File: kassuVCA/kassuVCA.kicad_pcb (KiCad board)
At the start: 2 copper layers, 140 parts, among them J201 Conn_02x05_Odd_Even, Q401 MMBT3904, Q402 MBT3904DW1, Q403 MBT3904DW1, Q404 MMBT3904, Q501 MMBT3904, Q502 MMBT3904, Q503 MBT3904DW1, Q504 MBT3904DW1, SW401 SW_DPDT_x2, SW402 SW_DPDT_x2, SW501 SW_DPDT_x2, SW502 SW_DPDT_x2, U301 TL074, U401 TL072, U402 TL072, U501 TL072, U502 TL072

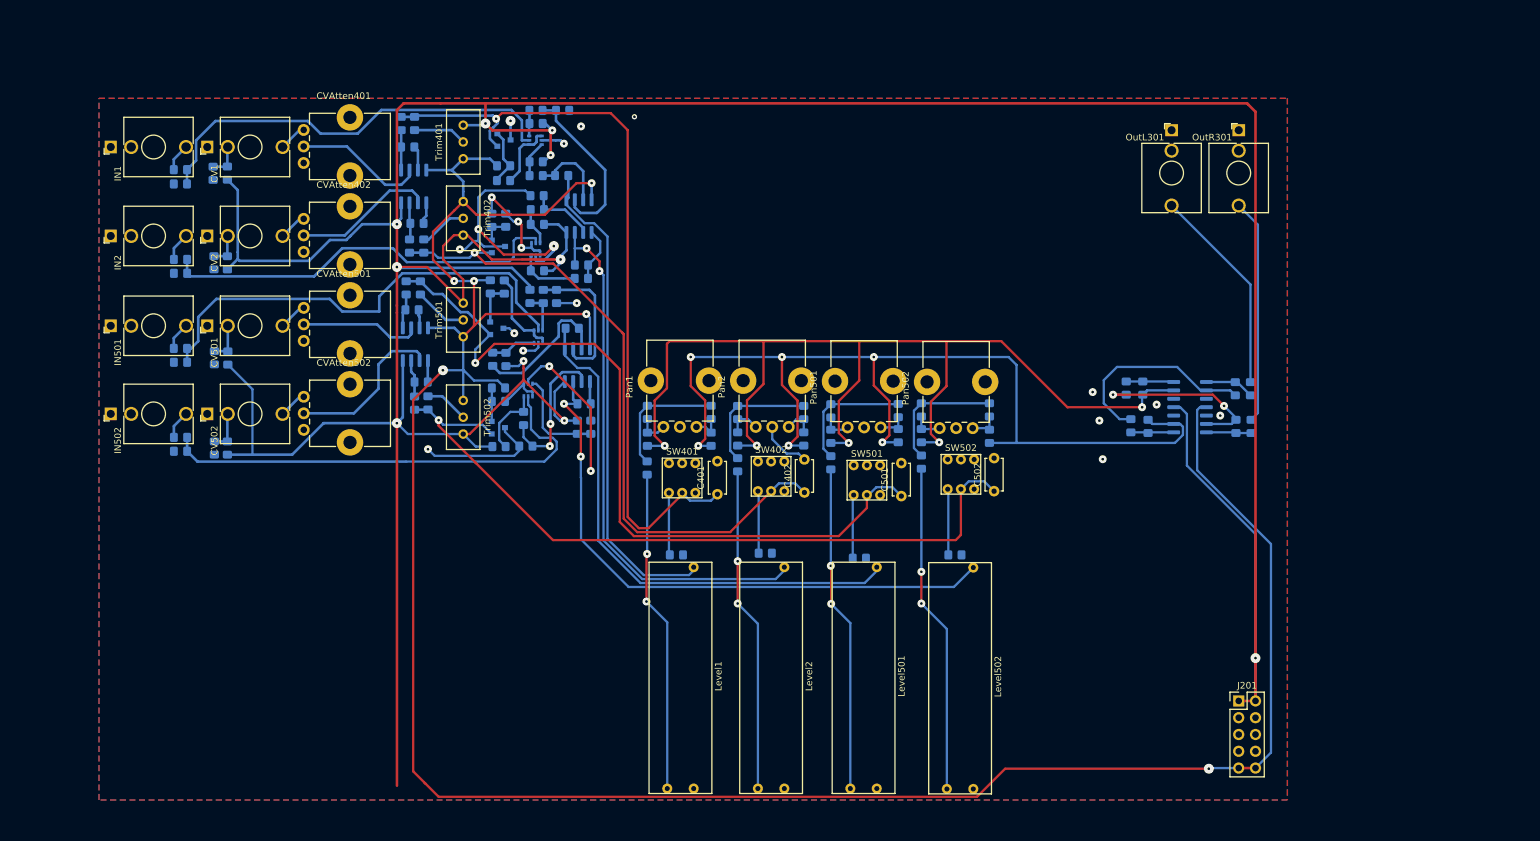
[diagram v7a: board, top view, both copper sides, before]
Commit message: mixer WIP, 8 channels, more or less
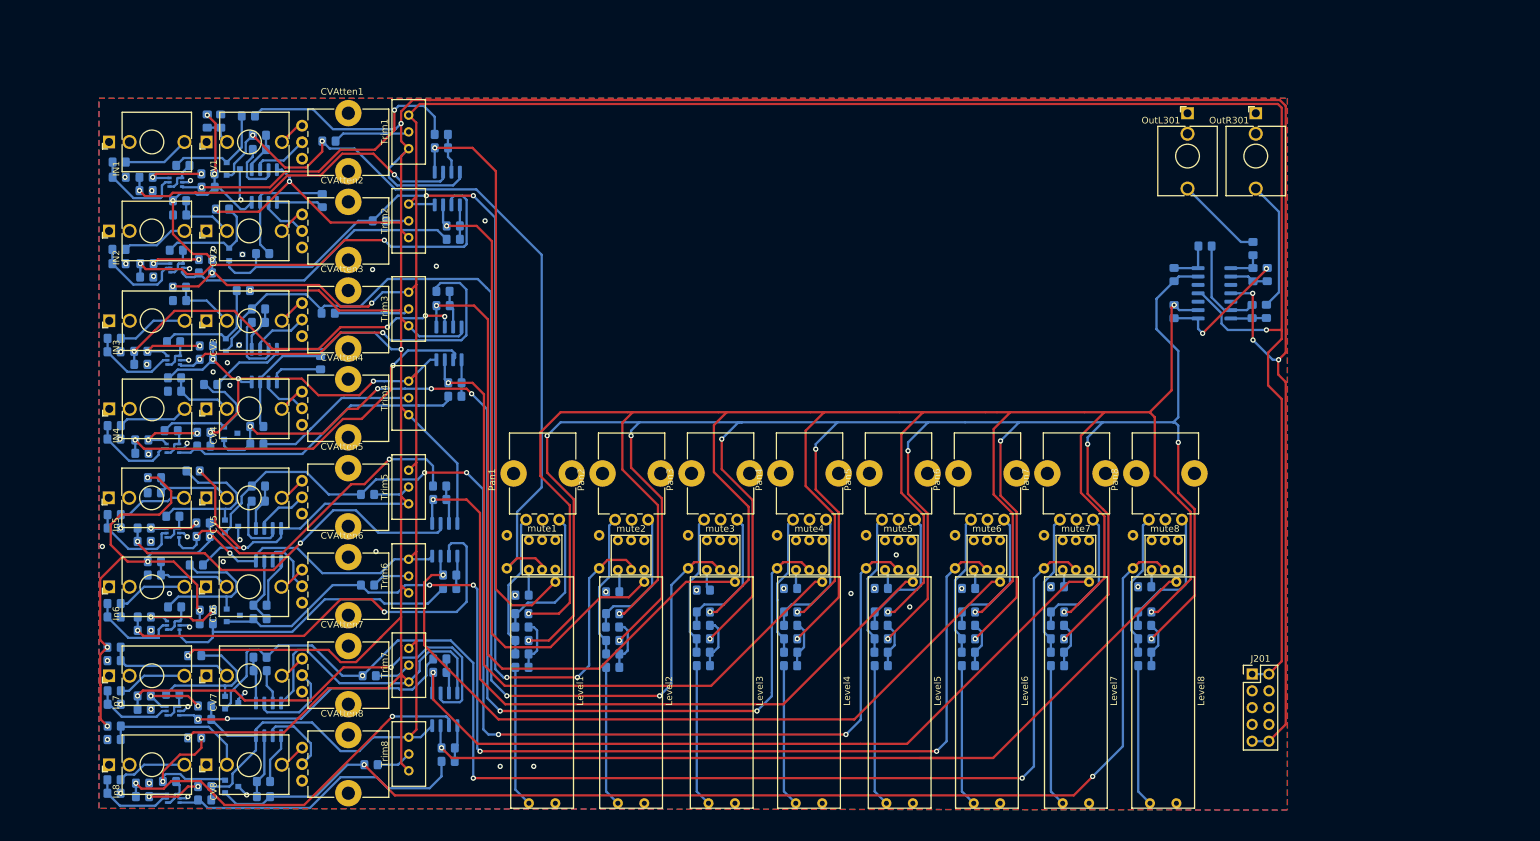
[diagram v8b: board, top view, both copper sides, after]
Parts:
- removed CV501, CV502, IN501, IN502: AudioJack2_SwitchT, Connector_Audio:Jack_3.5mm_QingPu_WQP-PJ398SM_Vertical_CircularHoles
- removed CVAtten401, CVAtten402, CVAtten501, CVAtten502, Pan501, Pan502: 100K, Potentiometer_THT:Potentiometer_Alps_RK09K_Single_Vertical
- removed Level501, Level502: 100K, MixerFootprints:A-1623_SlidePot
- removed SW401, SW402, SW501, SW502: SW_DPDT_x2, MixerFootprints:A-330-6mm-dpdt
- removed Trim401, Trim402, Trim501, Trim502: 100K, Potentiometer_THT:Potentiometer_Bourns_3296W_Vertical
- added C1: C, Capacitor_THT:C_Disc_D4.7mm_W2.5mm_P5.00mm, B.Cu at (141.7, 96.8)
- added C2: C, Capacitor_THT:C_Disc_D4.7mm_W2.5mm_P5.00mm, B.Cu at (155.2, 96.8)
- added C3: C, Capacitor_THT:C_Disc_D4.7mm_W2.5mm_P5.00mm, B.Cu at (168.7, 96.8)
- added C4: C, Capacitor_THT:C_Disc_D4.7mm_W2.5mm_P5.00mm, B.Cu at (182.1, 96.8)
- added CV3: AudioJack2_SwitchT, Connector_Audio:Jack_3.5mm_QingPu_WQP-PJ398SM_Vertical_CircularHoles, F.Cu at (41.9, 59.3)
- added CV4: AudioJack2_Switch, Connector_Audio:Jack_3.5mm_QingPu_WQP-PJ398SM_Vertical_CircularHoles, F.Cu at (41.9, 72.6)
- added CV5: AudioJack2_SwitchT, Connector_Audio:Jack_3.5mm_QingPu_WQP-PJ398SM_Vertical_CircularHoles, F.Cu at (41.9, 86.1)
- added CV6: AudioJack2_SwitchT, Connector_Audio:Jack_3.5mm_QingPu_WQP-PJ398SM_Vertical_CircularHoles, F.Cu at (41.9, 99.6)
- added CV7: AudioJack2_SwitchT, Connector_Audio:Jack_3.5mm_QingPu_WQP-PJ398SM_Vertical_CircularHoles, F.Cu at (41.9, 113.0)
- added CV8: AudioJack2_SwitchT, Connector_Audio:Jack_3.5mm_QingPu_WQP-PJ398SM_Vertical_CircularHoles, F.Cu at (41.9, 126.5)
- added CVAtten1: 100K, Potentiometer_THT:Potentiometer_Alps_RK09K_Single_Vertical, F.Cu at (56.4, 34.8)
- added CVAtten2: 100K, Potentiometer_THT:Potentiometer_Alps_RK09K_Single_Vertical, F.Cu at (56.4, 48.2)
- added CVAtten3: 100K, Potentiometer_THT:Potentiometer_Alps_RK09K_Single_Vertical, F.Cu at (56.4, 61.6)
- added CVAtten4: 100K, Potentiometer_THT:Potentiometer_Alps_RK09K_Single_Vertical, F.Cu at (56.4, 75.1)
- added CVAtten5: 100K, Potentiometer_THT:Potentiometer_Alps_RK09K_Single_Vertical, F.Cu at (56.4, 88.5)
- added CVAtten6: 100K, Potentiometer_THT:Potentiometer_Alps_RK09K_Single_Vertical, F.Cu at (56.4, 102.0)
- added CVAtten7: 100K, Potentiometer_THT:Potentiometer_Alps_RK09K_Single_Vertical, F.Cu at (56.4, 115.4)
- added CVAtten8: 100K, Potentiometer_THT:Potentiometer_Alps_RK09K_Single_Vertical, F.Cu at (56.4, 128.9)
- added IN3: AudioJack2_SwitchT, Connector_Audio:Jack_3.5mm_QingPu_WQP-PJ398SM_Vertical_CircularHoles, F.Cu at (27.2, 59.3)
- added IN4: AudioJack2_SwitchT, Connector_Audio:Jack_3.5mm_QingPu_WQP-PJ398SM_Vertical_CircularHoles, F.Cu at (27.2, 72.6)
- added In5: AudioJack2_SwitchT, Connector_Audio:Jack_3.5mm_QingPu_WQP-PJ398SM_Vertical_CircularHoles, F.Cu at (27.1, 86.1)
- added In6: AudioJack2_SwitchT, Connector_Audio:Jack_3.5mm_QingPu_WQP-PJ398SM_Vertical_CircularHoles, F.Cu at (27.2, 99.6)
- added In7: AudioJack2_SwitchT, Connector_Audio:Jack_3.5mm_QingPu_WQP-PJ398SM_Vertical_CircularHoles, F.Cu at (27.2, 113.0)
- added In8: AudioJack2_SwitchT, Connector_Audio:Jack_3.5mm_QingPu_WQP-PJ398SM_Vertical_CircularHoles, F.Cu at (27.2, 126.5)
- added Level3: 100K, MixerFootprints:A-1623_SlidePot, F.Cu at (119.9, 115.6)
- added Level4: 100K, MixerFootprints:A-1623_SlidePot, F.Cu at (133.1, 115.6)
- added Level5: 100K, MixerFootprints:A-1623_SlidePot, F.Cu at (146.8, 115.6)
- added Level6: 100K, MixerFootprints:A-1623_SlidePot, F.Cu at (160.0, 115.6)
- added Level7: 100K, MixerFootprints:A-1623_SlidePot, F.Cu at (173.5, 115.6)
- added Level8: 100K, MixerFootprints:A-1623_SlidePot, F.Cu at (186.7, 115.6)
- added Pan3: 100K, Potentiometer_THT:Potentiometer_Alps_RK09K_Single_Vertical, F.Cu at (122.2, 89.4)
- added Pan4: 100K, Potentiometer_THT:Potentiometer_Alps_RK09K_Single_Vertical, F.Cu at (135.7, 89.4)
- added Pan5: 100K, Potentiometer_THT:Potentiometer_Alps_RK09K_Single_Vertical, F.Cu at (149.1, 89.4)
- added Pan6: 100K, Potentiometer_THT:Potentiometer_Alps_RK09K_Single_Vertical, F.Cu at (162.6, 89.4)
- added Pan7: 100K, Potentiometer_THT:Potentiometer_Alps_RK09K_Single_Vertical, F.Cu at (176.1, 89.4)
- added Pan8: 100K, Potentiometer_THT:Potentiometer_Alps_RK09K_Single_Vertical, F.Cu at (189.5, 89.4)
- added Q1: MMBT3904, Package_TO_SOT_SMD:SOT-23, B.Cu at (45.7, 90.4)
- added Q2: MMBT3904, Package_TO_SOT_SMD:SOT-23, B.Cu at (46.0, 103.9)
- added Q3: MBT3904DW1, Package_TO_SOT_SMD:SOT-363_SC-70-6, B.Cu at (36.8, 91.4)
- added Q4: MBT3904DW1, Package_TO_SOT_SMD:SOT-363_SC-70-6, B.Cu at (36.9, 105.4)
- added Q5: MMBT3904, Package_TO_SOT_SMD:SOT-23, B.Cu at (45.7, 117.1)
- added Q6: MMBT3904, Package_TO_SOT_SMD:SOT-23, B.Cu at (45.7, 129.8)
- added Q7: MBT3904DW1, Package_TO_SOT_SMD:SOT-363_SC-70-6, B.Cu at (36.8, 118.4)
- added Q8: MBT3904DW1, Package_TO_SOT_SMD:SOT-363_SC-70-6, B.Cu at (36.9, 131.6)
- added R1: 220K, Resistor_SMD:R_0805_2012Metric_Pad1.20x1.40mm_HandSolder, B.Cu at (34.1, 83.1)
- added R10: 22K, Resistor_SMD:R_0805_2012Metric_Pad1.20x1.40mm_HandSolder, B.Cu at (50.0, 104.4)
- added R11: 22K, Resistor_SMD:R_0805_2012Metric_Pad1.20x1.40mm_HandSolder, B.Cu at (66.3, 85.6)
- added R12: 22K, Resistor_SMD:R_0805_2012Metric_Pad1.20x1.40mm_HandSolder, B.Cu at (66.3, 99.3)
- added R13: 1K, Resistor_SMD:R_0805_2012Metric_Pad1.20x1.40mm_HandSolder, B.Cu at (28.0, 90.7)
- added R14: 1K, Resistor_SMD:R_0805_2012Metric_Pad1.20x1.40mm_HandSolder, B.Cu at (144.0, 99.8)
- added R15: 1K, Resistor_SMD:R_0805_2012Metric_Pad1.20x1.40mm_HandSolder, B.Cu at (27.9, 104.1)
- added R16: 1K, Resistor_SMD:R_0805_2012Metric_Pad1.20x1.40mm_HandSolder, B.Cu at (157.2, 99.8)
- added R17: 10K, Resistor_SMD:R_0805_2012Metric_Pad1.20x1.40mm_HandSolder, B.Cu at (41.4, 91.9)
- added R18: 10K, Resistor_SMD:R_0805_2012Metric_Pad1.20x1.40mm_HandSolder, B.Cu at (41.9, 105.2)
- added R19: 22K, Resistor_SMD:R_0805_2012Metric_Pad1.20x1.40mm_HandSolder, B.Cu at (36.8, 88.9)
- added R2: 220K, Resistor_SMD:R_0805_2012Metric_Pad1.20x1.40mm_HandSolder, B.Cu at (34.0, 95.8)
- added R20: 10K, Resistor_SMD:R_0805_2012Metric_Pad1.20x1.40mm_HandSolder, B.Cu at (39.9, 82.0)
- added R21: 22K, Resistor_SMD:R_0805_2012Metric_Pad1.20x1.40mm_HandSolder, B.Cu at (37.1, 102.6)
- added R22: 10K, Resistor_SMD:R_0805_2012Metric_Pad1.20x1.40mm_HandSolder, B.Cu at (40.4, 96.3)
- added R23: 10K, Resistor_SMD:R_0805_2012Metric_Pad1.20x1.40mm_HandSolder, B.Cu at (41.4, 89.9)
- added R24: 10K, Resistor_SMD:R_0805_2012Metric_Pad1.20x1.40mm_HandSolder, B.Cu at (41.9, 103.1)
- added R25: 10K, Resistor_SMD:R_0805_2012Metric_Pad1.20x1.40mm_HandSolder, B.Cu at (77.2, 84.3)
- added R26: 10K, Resistor_SMD:R_0805_2012Metric_Pad1.20x1.40mm_HandSolder, B.Cu at (32.5, 90.7)
- added R27: 10K, Resistor_SMD:R_0805_2012Metric_Pad1.20x1.40mm_HandSolder, B.Cu at (78.7, 99.8)
- added R28: 10K, Resistor_SMD:R_0805_2012Metric_Pad1.20x1.40mm_HandSolder, B.Cu at (32.5, 104.1)
- added R29: 220K, Resistor_SMD:R_0805_2012Metric_Pad1.20x1.40mm_HandSolder, B.Cu at (32.5, 92.7)
- added R3: 100K, Resistor_SMD:R_0805_2012Metric_Pad1.20x1.40mm_HandSolder, B.Cu at (34.0, 85.3)
- added R30: 220K, Resistor_SMD:R_0805_2012Metric_Pad1.20x1.40mm_HandSolder, B.Cu at (32.5, 106.2)
- added R31: 220K, Resistor_SMD:R_0805_2012Metric_Pad1.20x1.40mm_HandSolder, B.Cu at (77.2, 86.4)
- added R32: 220K, Resistor_SMD:R_0805_2012Metric_Pad1.20x1.40mm_HandSolder, B.Cu at (78.7, 97.8)
- added R33: 220K, Resistor_SMD:R_0805_2012Metric_Pad1.20x1.40mm_HandSolder, B.Cu at (144.0, 111.5)
- added R34: 220K, Resistor_SMD:R_0805_2012Metric_Pad1.20x1.40mm_HandSolder, B.Cu at (157.2, 111.5)
- added R35: 22K, Resistor_SMD:R_0805_2012Metric_Pad1.20x1.40mm_HandSolder, B.Cu at (144.0, 109.5)
- added R36: 22K, Resistor_SMD:R_0805_2012Metric_Pad1.20x1.40mm_HandSolder, B.Cu at (144.0, 105.4)
- added R37: 22K, Resistor_SMD:R_0805_2012Metric_Pad1.20x1.40mm_HandSolder, B.Cu at (157.2, 109.5)
- added R38: 22K, Resistor_SMD:R_0805_2012Metric_Pad1.20x1.40mm_HandSolder, B.Cu at (157.2, 105.4)
- added R39: 22K, Resistor_SMD:R_0805_2012Metric_Pad1.20x1.40mm_HandSolder, B.Cu at (144.0, 107.4)
- added R4: 100K, Resistor_SMD:R_0805_2012Metric_Pad1.20x1.40mm_HandSolder, B.Cu at (34.0, 97.8)
- added R40: 22K, Resistor_SMD:R_0805_2012Metric_Pad1.20x1.40mm_HandSolder, B.Cu at (144.0, 103.4)
- added R41: 22K, Resistor_SMD:R_0805_2012Metric_Pad1.20x1.40mm_HandSolder, B.Cu at (157.2, 107.4)
- added R42: 22K, Resistor_SMD:R_0805_2012Metric_Pad1.20x1.40mm_HandSolder, B.Cu at (157.2, 103.4)
- added R43: 220K, Resistor_SMD:R_0805_2012Metric_Pad1.20x1.40mm_HandSolder, B.Cu at (27.9, 108.7)
- added R44: 220K, Resistor_SMD:R_0805_2012Metric_Pad1.20x1.40mm_HandSolder, B.Cu at (28.0, 120.7)
- added R45: 100K, Resistor_SMD:R_0805_2012Metric_Pad1.20x1.40mm_HandSolder, B.Cu at (27.9, 110.7)
- added R46: 100K, Resistor_SMD:R_0805_2012Metric_Pad1.20x1.40mm_HandSolder, B.Cu at (27.9, 122.7)
- added R47: 220K, Resistor_SMD:R_0805_2012Metric_Pad1.20x1.40mm_HandSolder, B.Cu at (28.0, 115.3)
- added R48: 220K, Resistor_SMD:R_0805_2012Metric_Pad1.20x1.40mm_HandSolder, B.Cu at (27.9, 128.8)
- added R49: 47K, Resistor_SMD:R_0805_2012Metric_Pad1.20x1.40mm_HandSolder, B.Cu at (50.0, 112.3)
- added R5: 220K, Resistor_SMD:R_0805_2012Metric_Pad1.20x1.40mm_HandSolder, B.Cu at (28.0, 88.6)
- added R50: 47K, Resistor_SMD:R_0805_2012Metric_Pad1.20x1.40mm_HandSolder, B.Cu at (50.5, 129.0)
- added R51: 22K, Resistor_SMD:R_0805_2012Metric_Pad1.20x1.40mm_HandSolder, B.Cu at (50.0, 110.2)
- added R52: 22K, Resistor_SMD:R_0805_2012Metric_Pad1.20x1.40mm_HandSolder, B.Cu at (50.5, 131.3)
- added R53: 22K, Resistor_SMD:R_0805_2012Metric_Pad1.20x1.40mm_HandSolder, B.Cu at (66.5, 113.0)
- added R54: 22K, Resistor_SMD:R_0805_2012Metric_Pad1.20x1.40mm_HandSolder, B.Cu at (66.8, 126.5)
- added R55: 1K, Resistor_SMD:R_0805_2012Metric_Pad1.20x1.40mm_HandSolder, B.Cu at (28.0, 117.3)
- added R56: 1K, Resistor_SMD:R_0805_2012Metric_Pad1.20x1.40mm_HandSolder, B.Cu at (170.7, 99.6)
- added R57: 1K, Resistor_SMD:R_0805_2012Metric_Pad1.20x1.40mm_HandSolder, B.Cu at (27.9, 130.8)
- added R58: 1K, Resistor_SMD:R_0805_2012Metric_Pad1.20x1.40mm_HandSolder, B.Cu at (183.9, 99.6)
- added R59: 10K, Resistor_SMD:R_0805_2012Metric_Pad1.20x1.40mm_HandSolder, B.Cu at (41.6, 119.6)
- added R6: 220K, Resistor_SMD:R_0805_2012Metric_Pad1.20x1.40mm_HandSolder, B.Cu at (27.9, 102.1)
- added R60: 10K, Resistor_SMD:R_0805_2012Metric_Pad1.20x1.40mm_HandSolder, B.Cu at (41.6, 131.8)
- added R61: 22K, Resistor_SMD:R_0805_2012Metric_Pad1.20x1.40mm_HandSolder, B.Cu at (36.8, 115.8)
- added R62: 10K, Resistor_SMD:R_0805_2012Metric_Pad1.20x1.40mm_HandSolder, B.Cu at (40.1, 110.0)
- added R63: 22K, Resistor_SMD:R_0805_2012Metric_Pad1.20x1.40mm_HandSolder, B.Cu at (36.3, 129.0)
- added R64: 10K, Resistor_SMD:R_0805_2012Metric_Pad1.20x1.40mm_HandSolder, B.Cu at (40.1, 122.4)
- added R65: 10K, Resistor_SMD:R_0805_2012Metric_Pad1.20x1.40mm_HandSolder, B.Cu at (41.6, 117.6)
- added R66: 10K, Resistor_SMD:R_0805_2012Metric_Pad1.20x1.40mm_HandSolder, B.Cu at (41.6, 129.8)
- added R67: 10K, Resistor_SMD:R_0805_2012Metric_Pad1.20x1.40mm_HandSolder, B.Cu at (77.2, 110.5)
- added R68: 10K, Resistor_SMD:R_0805_2012Metric_Pad1.20x1.40mm_HandSolder, B.Cu at (32.5, 116.1)
- added R69: 10K, Resistor_SMD:R_0805_2012Metric_Pad1.20x1.40mm_HandSolder, B.Cu at (78.5, 126.0)
- added R7: 47K, Resistor_SMD:R_0805_2012Metric_Pad1.20x1.40mm_HandSolder, B.Cu at (49.8, 86.6)
- added R70: 10K, Resistor_SMD:R_0805_2012Metric_Pad1.20x1.40mm_HandSolder, B.Cu at (32.2, 131.3)
- added R71: 220K, Resistor_SMD:R_0805_2012Metric_Pad1.20x1.40mm_HandSolder, B.Cu at (32.5, 118.1)
- added R72: 220K, Resistor_SMD:R_0805_2012Metric_Pad1.20x1.40mm_HandSolder, B.Cu at (32.2, 129.3)
- added R73: 220K, Resistor_SMD:R_0805_2012Metric_Pad1.20x1.40mm_HandSolder, B.Cu at (77.2, 112.5)
- added R74: 220K, Resistor_SMD:R_0805_2012Metric_Pad1.20x1.40mm_HandSolder, B.Cu at (78.5, 124.0)
- added R75: 220K, Resistor_SMD:R_0805_2012Metric_Pad1.20x1.40mm_HandSolder, B.Cu at (170.7, 111.5)
- added R76: 220K, Resistor_SMD:R_0805_2012Metric_Pad1.20x1.40mm_HandSolder, B.Cu at (183.9, 111.5)
- added R77: 22K, Resistor_SMD:R_0805_2012Metric_Pad1.20x1.40mm_HandSolder, B.Cu at (170.7, 109.5)
- added R78: 22K, Resistor_SMD:R_0805_2012Metric_Pad1.20x1.40mm_HandSolder, B.Cu at (170.7, 105.4)
- added R79: 22K, Resistor_SMD:R_0805_2012Metric_Pad1.20x1.40mm_HandSolder, B.Cu at (183.9, 109.5)
- added R8: 47K, Resistor_SMD:R_0805_2012Metric_Pad1.20x1.40mm_HandSolder, B.Cu at (50.0, 102.4)
- added R80: 22K, Resistor_SMD:R_0805_2012Metric_Pad1.20x1.40mm_HandSolder, B.Cu at (183.9, 105.4)
- added R81: 22K, Resistor_SMD:R_0805_2012Metric_Pad1.20x1.40mm_HandSolder, B.Cu at (170.7, 107.4)
- added R82: 22K, Resistor_SMD:R_0805_2012Metric_Pad1.20x1.40mm_HandSolder, B.Cu at (170.7, 103.4)
- added R83: 22K, Resistor_SMD:R_0805_2012Metric_Pad1.20x1.40mm_HandSolder, B.Cu at (183.9, 107.4)
- added R84: 22K, Resistor_SMD:R_0805_2012Metric_Pad1.20x1.40mm_HandSolder, B.Cu at (183.9, 103.4)
- added R9: 22K, Resistor_SMD:R_0805_2012Metric_Pad1.20x1.40mm_HandSolder, B.Cu at (49.8, 84.3)
- added Trim1: 100K, Potentiometer_THT:Potentiometer_Bourns_3296W_Vertical, F.Cu at (72.5, 28.2)
- added Trim2: 100K, Potentiometer_THT:Potentiometer_Bourns_3296W_Vertical, F.Cu at (72.5, 41.7)
- added Trim3: 100K, Potentiometer_THT:Potentiometer_Bourns_3296W_Vertical, F.Cu at (72.5, 55.0)
- added Trim4: 100K, Potentiometer_THT:Potentiometer_Bourns_3296W_Vertical, F.Cu at (72.5, 68.5)
- added Trim5: 100K, Potentiometer_THT:Potentiometer_Bourns_3296W_Vertical, F.Cu at (72.5, 81.9)
- added Trim6: 100K, Potentiometer_THT:Potentiometer_Bourns_3296W_Vertical, F.Cu at (72.5, 95.4)
- added Trim7: 100K, Potentiometer_THT:Potentiometer_Bourns_3296W_Vertical, F.Cu at (72.5, 108.9)
- added Trim8: 100K, Potentiometer_THT:Potentiometer_Bourns_3296W_Vertical, F.Cu at (72.5, 122.3)
- added U1: TL072, Package_SO:SOIC-8_3.9x4.9mm_P1.27mm, B.Cu at (51.3, 93.2)
- added U2: TL072, Package_SO:SOIC-8_3.9x4.9mm_P1.27mm, B.Cu at (78.0, 92.5)
- added U3: TL072, Package_SO:SOIC-8_3.9x4.9mm_P1.27mm, B.Cu at (51.3, 119.6)
- added U4: TL072, Package_SO:SOIC-8_3.9x4.9mm_P1.27mm, B.Cu at (78.0, 118.1)
- added mute1: SW_DPDT_x2, MixerFootprints:A-330-6mm-dpdt, F.Cu at (92.7, 94.7)
- added mute2: SW_DPDT_x2, MixerFootprints:A-330-6mm-dpdt, F.Cu at (106.2, 94.8)
- added mute3: SW_DPDT_x2, MixerFootprints:A-330-6mm-dpdt, F.Cu at (119.6, 94.8)
- added mute4: SW_DPDT_x2, MixerFootprints:A-330-6mm-dpdt, F.Cu at (133.1, 94.8)
- added mute5: mute5, MixerFootprints:A-330-6mm-dpdt, F.Cu at (146.6, 94.8)
- added mute6: SW_DPDT_x2, MixerFootprints:A-330-6mm-dpdt, F.Cu at (160.0, 94.8)
- added mute7: mute7, MixerFootprints:A-330-6mm-dpdt, F.Cu at (173.5, 94.8)
- added mute8: SW_DPDT_x2, MixerFootprints:A-330-6mm-dpdt, F.Cu at (186.9, 94.8)
- C401, C402, C501, C502: moved to B.Cu
- CV2: value AudioJack2_SwitchT -> AudioJack2_Switch
- moved R429 64.2 mm to (32.8, 39.6)
- moved R529 63.7 mm to (32.0, 65.9), turned to 180 degrees
- moved R526 61.5 mm to (32.0, 63.9), turned to 0 degrees
- moved R430 60.3 mm to (32.9, 52.7), turned to 180 degrees
- moved R426 59.9 mm to (32.8, 37.6), turned to 0 degrees
- moved R428 59.6 mm to (32.9, 50.7), turned to 0 degrees
- moved R530 58.1 mm to (32.1, 79.4), turned to 180 degrees
- moved R528 57.9 mm to (32.1, 77.3), turned to 0 degrees
- moved R518 56.6 mm to (41.5, 78.3), turned to 180 degrees
- moved Q503 55.3 mm to (37.0, 65.3), turned to 0 degrees
- moved Q402 54.8 mm to (37.3, 38.4)
- moved Q504 54.5 mm to (36.8, 78.6), turned to 0 degrees
- moved Q403 54.4 mm to (37.4, 51.3), turned to 0 degrees
- moved R519 50.7 mm to (36.9, 62.5), turned to 180 degrees
- moved R424 50.5 mm to (41.8, 50.0)
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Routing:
- net -12V: track 382.8 -> 693.1 mm, vias 7 -> 12
- net Level1R: track 162.4 -> 426.2 mm, vias 5 -> 16
- net Level1L: track 149.0 -> 401.6 mm, vias 6 -> 9
- net Net-(C3-Pad1): track 0.00 -> 190.4 mm, vias 0 -> 3
- net Net-(C4-Pad1): track 0.00 -> 177.3 mm, vias 0 -> 2
- net Net-(C1-Pad1): track 0.00 -> 172.1 mm, vias 0 -> 4
- net Net-(C2-Pad1): track 0.00 -> 170.7 mm, vias 0 -> 4
- net Net-(Level8-Pad3): track 0.00 -> 131.9 mm, vias 0 -> 1
- net Net-(Level7-Pad3): track 0.00 -> 119.5 mm, vias 0 -> 1
- net Net-(Level6-Pad3): track 0.00 -> 116.2 mm, vias 0 -> 1
- net Net-(Level5-Pad3): track 0.00 -> 111.5 mm, vias 0 -> 1
- net GND: track 106.1 -> 22.2 mm, vias 18 -> 55
- net Net-(R28-Pad1): track 0.00 -> 68.9 mm, vias 0 -> 2
- net Net-(R68-Pad1): track 0.00 -> 67.0 mm, vias 0 -> 2
- net Net-(R70-Pad1): track 0.00 -> 58.5 mm, vias 0 -> 2
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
